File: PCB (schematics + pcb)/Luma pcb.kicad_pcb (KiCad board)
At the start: 2 copper layers, 21 parts, among them J1 Conn_01x04_Pin, SW1 SW_Push, SW2 SW_Push, SW3 SW_Push, SW4 SW_Push, SW5 SW_Push, SW6 RotaryEncoder_Switch, U1 MOUDLE-SEEEDUINO-XIAO

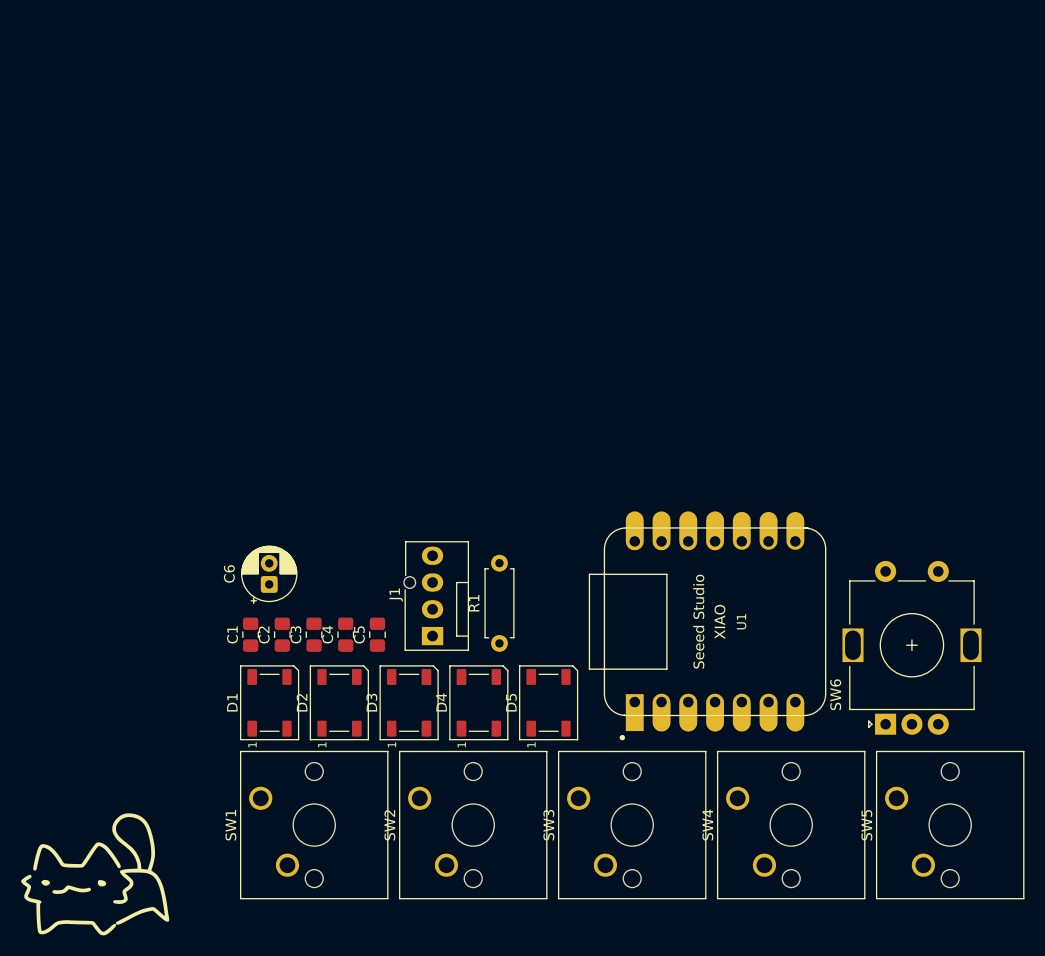
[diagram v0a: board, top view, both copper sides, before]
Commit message: Add QMK firmware matching PCB netlist, CAD case files, and PCB updates
Firmware (XIAO RP2040):
- Add keyboard.json with correct pins traced from the PCB netlist:
  switches on GP26/GP27/GP28/GP29/GP4, encoder on GP0/GP1 with push
  button on GP2, OLED I2C on GP6/GP7, 5x SK6812 RGB LEDs on GP3
- Fix keymap.c: invalid X_LSHIFT keycode, KC_NO interception replaced
  with a proper ANIM_CYCLE keycode, encoder push mapped to mute
- Add three animated OLED modes (scanner, equalizer, breathing logo)
  with a live last-action status line
- Enable RGBLIGHT for the onboard LED chain

Also add CAD case STEP files and gitignore editor auto-backups.

Co-Authored-By: Claude Fable 5 <noreply@anthropic.com>
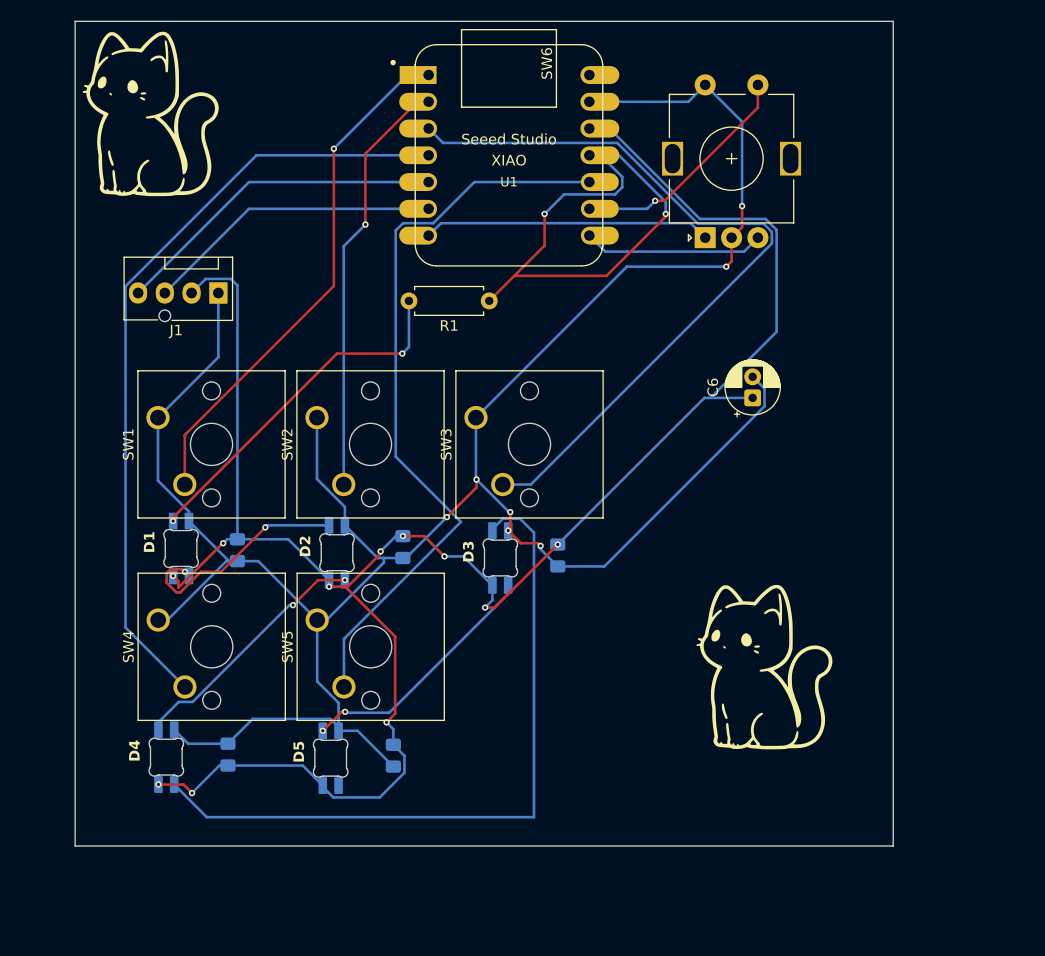
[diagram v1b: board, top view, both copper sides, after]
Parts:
- removed the G*** at (78.0, 139.0)
- added G***: LOGO, LOGO, F.Cu at (83.0, 65.0)
- added G***: LOGO, LOGO, F.Cu at (141.2, 117.5)
- C1, C2, C3, C4, C5: moved to B.Cu
- D1, D2, D3, D4, D5: value WS2812B -> SK6812MINI-E; footprint LED_SMD:LED_WS2812B_PLCC4_5.0x5.0mm_P3.2mm -> footprints:SK6812MINI-E_fixed
- moved SW4 57.5 mm to (84.1, 114.3)
- moved SW5 57.5 mm to (99.2, 114.3)
- moved SW6 49.3 mm to (136.0, 78.0)
- moved C6 49.2 mm to (140.5, 93.2)
- moved U1 48.4 mm to (117.4, 70.2), turned to 0 degrees
- moved J1 38.4 mm to (89.8, 83.2), turned to 180 degrees
- moved SW1 37.4 mm to (84.1, 95.1)
- moved SW2 37.4 mm to (99.2, 95.1)
- moved SW3 37.4 mm to (114.2, 95.1)
- moved R1 32.5 mm to (115.5, 84.0), turned to 180 degrees
- moved D4 30.0 mm to (85.0, 127.3)
- moved C2 27.2 mm to (122.0, 108.2), turned to -90 degrees
- moved D5 21.2 mm to (100.6, 127.4)
- moved D1 16.8 mm to (86.4, 107.5)
- moved D3 16.3 mm to (116.7, 108.4)
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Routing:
- net GND: track 0.00 -> 233.0 mm, vias 0 -> 7
- net Net-(D1-VDD): track 0.00 -> 192.0 mm, vias 0 -> 11
- net Net-(U1-PA11_A3_D3): track 0.00 -> 74.3 mm
- net Net-(U1-PA10_A2_D2): track 0.00 -> 72.8 mm
- net Net-(U1-PA5_A9_D9_MISO): track 0.00 -> 70.8 mm
- net Net-(D3-DIN): track 0.00 -> 67.5 mm
- net Net-(U1-PA6_A10_D10_MOSI): track 0.00 -> 51.0 mm, vias 0 -> 2
- net Net-(U1-PA02_A0_D0): track 0.00 -> 49.6 mm, vias 0 -> 1
- net Net-(U1-PA4_A1_D1): track 0.00 -> 40.3 mm, vias 0 -> 1
- net Net-(D1-DIN): track 0.00 -> 33.8 mm, vias 0 -> 2
- net Net-(J1-Pin_4): track 0.00 -> 31.9 mm
- net Net-(J1-Pin_3): track 0.00 -> 28.3 mm
- net Net-(U1-PB08_A6_D6_TX): track 0.00 -> 27.3 mm
- net Net-(D2-DOUT): track 0.00 -> 24.0 mm, vias 0 -> 2
- net Net-(D3-DOUT): track 0.00 -> 23.9 mm, vias 0 -> 2
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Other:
- board outline added: 77.6 x 78.3 mm
